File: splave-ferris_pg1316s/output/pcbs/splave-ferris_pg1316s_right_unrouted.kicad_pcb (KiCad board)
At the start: 2 copper layers, 117.9 x 85.9 mm, 37 parts

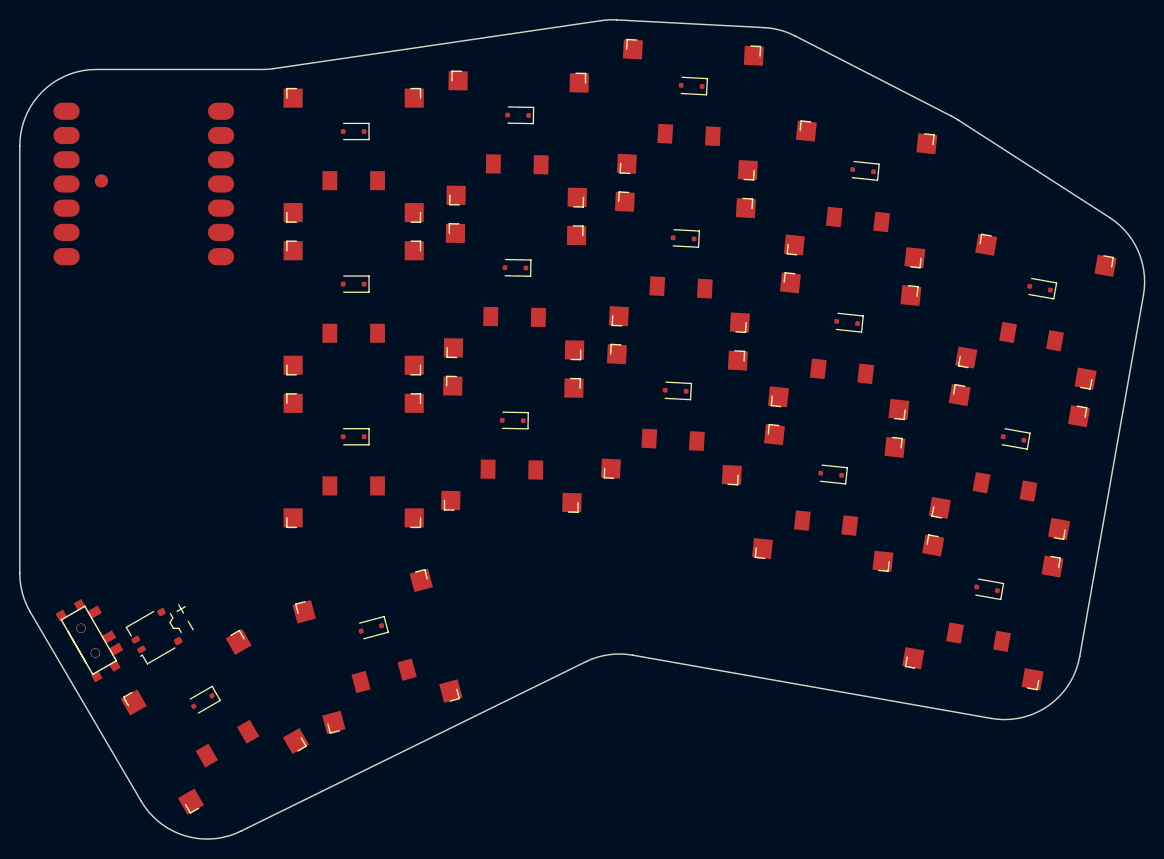
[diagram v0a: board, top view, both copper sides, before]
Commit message: Add stablizer holes to PG1316S footprint, regenerate PCB files.
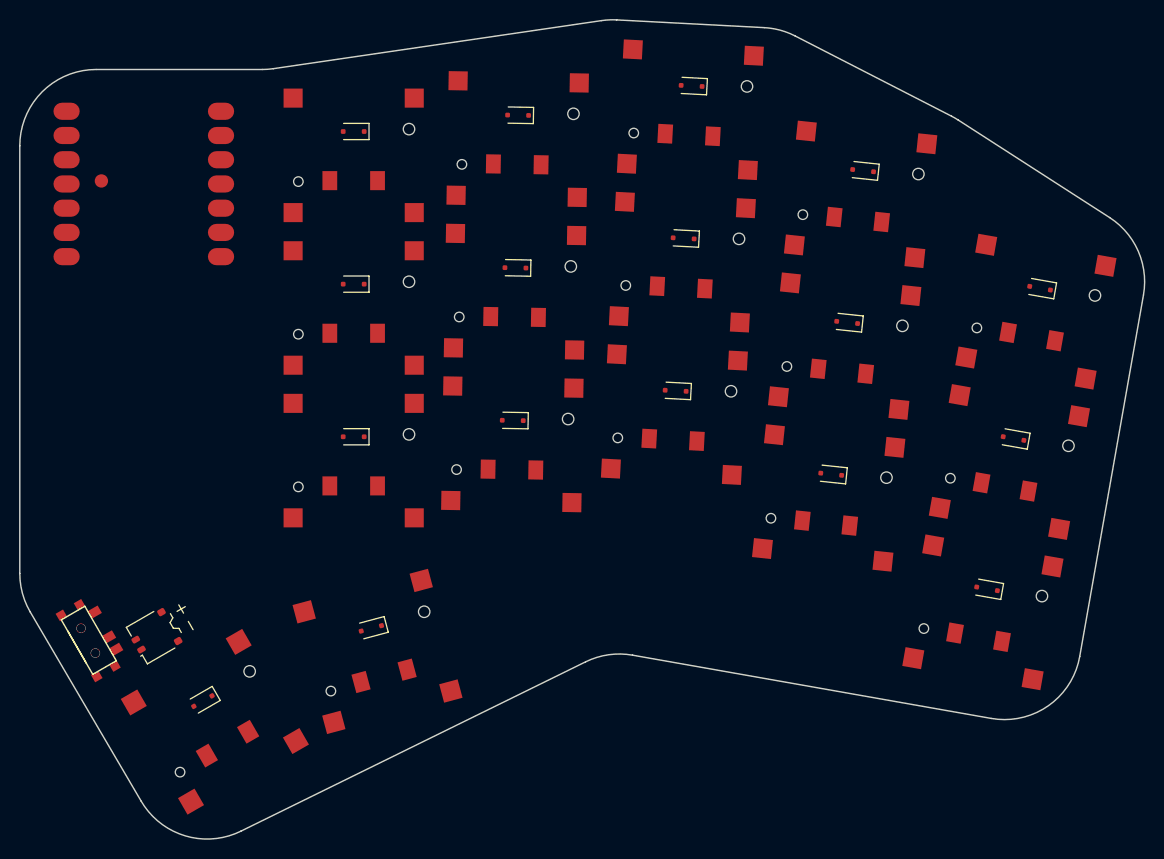
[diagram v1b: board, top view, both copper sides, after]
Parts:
- S1, S10, S11, S12, S13, S14, S15, S16, S17, S2, S3, S4, S5, S6, S7, S8, S9: footprint PG1316S -> CPG1316S01D02_mikeholscher
